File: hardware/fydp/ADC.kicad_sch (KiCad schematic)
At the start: 31 parts, among them J20 Conn_01x07_Pin, U34 LTC2353ILX-16-PBF

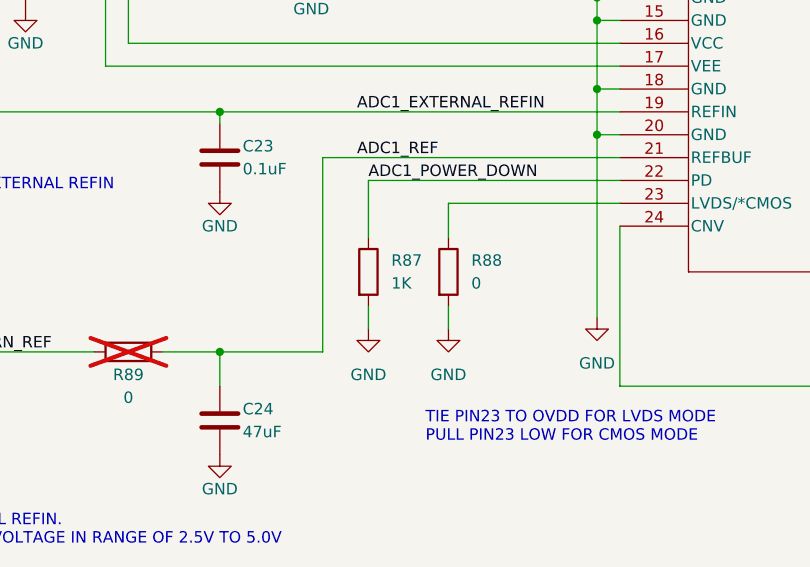
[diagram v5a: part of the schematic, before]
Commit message: Adding JLCPCB BOM notes
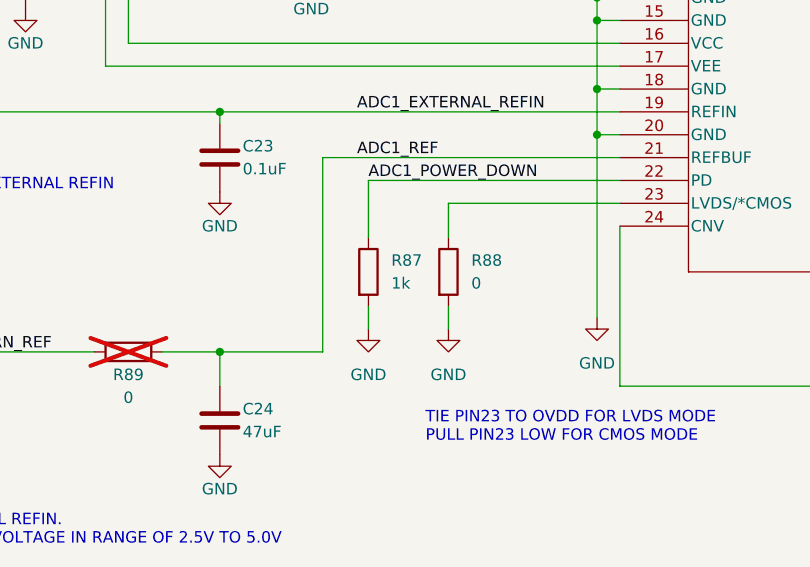
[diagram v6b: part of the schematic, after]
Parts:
- C23: Comment (none) -> 0.1 µF ±10% 50V Ceramic Capacitor X7R 0805 (2012 Metric); LCSC (none) -> C49678; MPN (none) -> CC0805KRX7R9BB104
- C23: Comment (none) -> 2.2 µF ±10% 25V Ceramic Capacitor X7R 0805 (2012 Metric); LCSC (none) -> C277470; MPN (none) -> CC0805KKX7R8BB225
- C24: Comment (none) -> 47 µF ±20% 6.3V Ceramic Capacitor X5R 0805 (2012 Metric); LCSC (none) -> C109461; MPN (none) -> CC0805MKX5R5BB476
- R1: Comment (none) -> 4.7 kOhms ±1% 0.125W, 1/8W Chip Resistor 0805 (2012 Metric)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; LCSC (none) -> C60816; MPN (none) -> RC0805FR-074K7L
- R62: Comment (none) -> 100 Ohms ±1% 0.125W, 1/8W Chip Resistor 0805 (2012 Metric) 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; LCSC (none) -> C105577; MPN (none) -> RC0805FR-07100RL
- R86, R88, R89: Comment (none) -> 0 Ohms Jumper Chip Resistor 0805 (2012 Metric) Moisture Res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; LCSC (none) -> C96345; MPN (none) -> RC0805JR-070RL
- R87: value 1K -> 1k; Comment (none) -> 1 kOhms ±1% 0.125W, 1/8W Chip Resistor 0805 (2012 Metric) M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; LCSC (none) -> C95781; MPN (none) -> RC0805FR-071KL

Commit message: Updating BOM some more
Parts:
- J20: Comment (none) -> Connector Header Through Hole 7 position 0.100" (2.54mm); MPN (none) -> TSW-107-07-G-S
- U34: Comment (none) -> 16 Bit Analog to Digital Converter 2 Input 1 SAR 48-LQFP (7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; MPN (none) -> LTC2353ILX-16#PBF
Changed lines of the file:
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@@
       (effects (font (size 1.27 1.27)) hide)
     )
-    (property "Datasheet" "~" (at 27.94 176.53 0)
+    (property "Datasheet" "https://suddendocs.samtec.com/catalog_english/tsw_th.pdf" (at 27.94 176.53 0)
+      (effects (font (size 1.27 1.27)) hide)
+    )
+    (property "Comment" "Connector Header Through Hole 7 position 0.100\" (2.54mm)" (at 27.94 176.53 0)
+      (effects (font (size 1.27 1.27)) hide)
+    )
+    (property "MPN" "TSW-107-07-G-S" (at 27.94 176.53 0)
       (effects (font (size 1.27 1.27)) hide)
     )
@@
       (effects (font (size 1.27 1.27) italic) hide)
     )
-    (property "Datasheet" "LTC2353ILX-16-PBF" (at 116.84 44.45 0)
+    (property "Datasheet" "https://www.analog.com/media/en/technical-documentation/data-sheets/235316f.pdf" (at 116.84 44.45 0)
       (effects (font (size 1.27 1.27) italic) hide)
     )
-    (pin "1")
+    (property "Comment" "16 Bit Analog to Digital Converter 2 Input 1 SAR 48-LQFP (7x7)" (at 116.84 44.45 0)
+      (effects (font (size 1.27 1.27)) hide)
+    )
+    (property "MPN" "LTC2353ILX-16#PBF" (at 116.84 44.45 0)
+      (effects (font (size 1.27 1.27)) hide)
+    )
+    (pin "1")

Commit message: Fixed footprints
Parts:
- J20: value Conn_01x07_Pin -> TSW-107-07-G-S
- U34: value LTC2353ILX-16-PBF -> LTC2353ILX-16#PBF
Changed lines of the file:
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@@
       (effects (font (size 1.27 1.27)))
     )
-    (property "Value" "Conn_01x07_Pin" (at 28.575 166.37 0)
+    (property "Value" "TSW-107-07-G-S" (at 28.575 166.37 0)
       (effects (font (size 1.27 1.27)))
     )
@@
       (effects (font (size 1.524 1.524)))
     )
-    (property "Value" "LTC2353ILX-16-PBF" (at 149.86 36.83 0)
+    (property "Value" "LTC2353ILX-16#PBF" (at 149.86 36.83 0)
       (effects (font (size 1.524 1.524)))
     )
